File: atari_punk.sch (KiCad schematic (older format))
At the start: 11 parts, among them J1 Conn_01x02_MountingPin, J2 Conn_01x02_MountingPin, U1 NE555P, U2 NE555P

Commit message: Added resistors. Added big Niubit logo. Added holes for mounting.
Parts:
- removed J1, J2: Conn_01x02_MountingPin, Connector_PinHeader_2.54mm:PinHeader_1x02_P2.54mm_Vertical, symbol Connector_Generic_MountingPin:Conn_01x02_MountingPin
- added J1, J2: Conn_01x02_Male, Connector_PinHeader_2.54mm:PinHeader_1x02_P2.54mm_Vertical, symbol Connector:Conn_01x02_Male
- added R5, R6: 1K, Resistor_THT:R_Axial_DIN0207_L6.3mm_D2.5mm_P10.16mm_Horizontal, symbol Device:R
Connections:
- net +9V: now also J1.2 (Pin_2)
- net AUDIO: now also J2.2 (Pin_2)
- net GND: now also J1.1 (Pin_1), J2.1 (Pin_1)
- net at R2.2, U1.7 (DIS): now also R5.1; no longer R1.2
- net at C3.1, U2.6 (THR), U2.7 (DIS): now also R6.1; no longer R4.2
- new net: R1.2, R5.2
- new net: R4.2, R6.2
- no-connect marks 4 -> 2
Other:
- moved on the sheet: R2, R4
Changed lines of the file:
@@
 L Device:R R2
 U 1 1 5FE47346
-P 3000 2500
-F 0 "R2" V 2793 2500 50  0000 C CNN
-F 1 "1K" V 2884 2500 50  0000 C CNN
-F 2 "Resistor_THT:R_Axial_DIN0207_L6.3mm_D2.5mm_P10.16mm_Horizontal" V 2930 2500 50  0001 C CNN
-F 3 "~" H 3000 2500 50  0001 C CNN
-	1    3000 2500
+P 3000 2700
+F 0 "R2" V 2793 2700 50  0000 C CNN
+F 1 "1K" V 2884 2700 50  0000 C CNN
+F 2 "Resistor_THT:R_Axial_DIN0207_L6.3mm_D2.5mm_P10.16mm_Horizontal" V 2930 2700 50  0001 C CNN
+F 3 "~" H 3000 2700 50  0001 C CNN
+	1    3000 2700
 	-1   0    0    1
 $EndComp
@@
 L power:+9V #PWR011
 U 1 1 5FE7EA0E
-P 5200 1450
-F 0 "#PWR011" H 5200 1300 50  0001 C CNN
-F 1 "+9V" H 5215 1623 50  0000 C CNN
-F 2 "" H 5200 1450 50  0001 C CNN
-F 3 "" H 5200 1450 50  0001 C CNN
-	1    5200 1450
+P 5900 1450
+F 0 "#PWR011" H 5900 1300 50  0001 C CNN
+F 1 "+9V" H 5915 1623 50  0000 C CNN
+F 2 "" H 5900 1450 50  0001 C CNN
+F 3 "" H 5900 1450 50  0001 C CNN
+	1    5900 1450
 	1    0    0    -1
 $EndComp
@@
 L Device:R_Variable R4
 U 1 1 5FE4885F
-P 5200 1700
-F 0 "R4" H 5328 1746 50  0000 L CNN
-F 1 "500K" H 5328 1655 50  0000 L CNN
-F 2 "Potentiometer_THT:Potentiometer_Alpha_RD901F-40-00D_Single_Vertical" V 5130 1700 50  0001 C CNN
-F 3 "~" H 5200 1700 50  0001 C CNN
-	1    5200 1700
+P 5900 1700
+F 0 "R4" H 6028 1746 50  0000 L CNN
+F 1 "500K" H 6028 1655 50  0000 L CNN
+F 2 "Potentiometer_THT:Potentiometer_Alpha_RD901F-40-00D_Single_Vertical" V 5830 1700 50  0001 C CNN
+F 3 "~" H 5900 1700 50  0001 C CNN
+	1    5900 1700
 	1    0    0    -1
 $EndComp
@@
 	3000 1450 3000 1550
 Wire Wire Line
-	3000 1850 3000 1950
-Wire Wire Line
-	2550 1950 3000 1950
-Connection ~ 3000 1950
-Wire Wire Line
-	3000 1950 3000 2350
-Wire Wire Line
-	3000 2650 3000 2900
+	3000 2850 3000 2900
 Wire Wire Line
 	3000 2900 2650 2900
@@
 	4800 1950 4900 1950
 Wire Wire Line
-	5200 1950 5200 1850
-Connection ~ 5200 1950
-Wire Wire Line
-	5200 1450 5200 1550
+	5900 1450 5900 1550
 Wire Wire Line
 	5200 2400 5200 2450
@@
 Wire Wire Line
 	4900 1950 5200 1950
-$Comp
-L Connector_Generic_MountingPin:Conn_01x02_MountingPin J1
-U 1 1 5FEDC132
-P 1750 3550
-F 0 "J1" H 1838 3464 50  0000 L CNN
-F 1 "Conn_01x02_MountingPin" H 1450 3650 50  0000 L CNN
-F 2 "Connector_PinHeader_2.54mm:PinHeader_1x02_P2.54mm_Vertical" H 1750 3550 50  0001 C CNN
-F 3 "~" H 1750 3550 50  0001 C CNN
-	1    1750 3550
-	-1   0    0    1
-$EndComp
-$Comp
-L Connector_Generic_MountingPin:Conn_01x02_MountingPin J2
-U 1 1 5FEDD85A
-P 4350 3550
-F 0 "J2" H 4438 3464 50  0000 L CNN
-F 1 "Conn_01x02_MountingPin" H 4050 3650 50  0000 L CNN
-F 2 "Connector_PinHeader_2.54mm:PinHeader_1x02_P2.54mm_Vertical" H 4350 3550 50  0001 C CNN
-F 3 "~" H 4350 3550 50  0001 C CNN
-	1    4350 3550
-	-1   0    0    1
-$EndComp
 $Comp
 L power:+9V #PWR01
@@
 	1    0    0    -1
 $EndComp
-Text GLabel 4800 3450 2    50   Input ~ 0
+Text GLabel 4800 3450 0    50   Input ~ 0
 AUDIO
 Text GLabel 5750 1000 2    50   Output ~ 0
@@
 	5350 1000 5750 1000
 Wire Wire Line
-	1950 3550 2150 3550
+	4800 3550 4800 3650
+$Comp
+L Device:R R5
+U 1 1 608860B0
+P 3000 2100
+F 0 "R5" V 2793 2100 50  0000 C CNN
+F 1 "1K" V 2884 2100 50  0000 C CNN
+F 2 "Resistor_THT:R_Axial_DIN0207_L6.3mm_D2.5mm_P10.16mm_Horizontal" V 2930 2100 50  0001 C CNN
+F 3 "~" H 3000 2100 50  0001 C CNN
+	1    3000 2100
+	-1   0    0    1
+$EndComp
+Wire Wire Line
+	3000 1950 3000 1850
+Wire Wire Line
+	3000 2250 3000 2400
+Wire Wire Line
+	2550 1950 2800 1950
+Wire Wire Line
+	2800 1950 2800 2400
+Wire Wire Line
+	2800 2400 3000 2400
+Connection ~ 3000 2400
+Wire Wire Line
+	3000 2400 3000 2550
+$Comp
+L Device:R R6
+U 1 1 6089116C
+P 5600 1950
+F 0 "R6" V 5393 1950 50  0000 C CNN
+F 1 "1K" V 5484 1950 50  0000 C CNN
+F 2 "Resistor_THT:R_Axial_DIN0207_L6.3mm_D2.5mm_P10.16mm_Horizontal" V 5530 1950 50  0001 C CNN
+F 3 "~" H 5600 1950 50  0001 C CNN
+	1    5600 1950
+	0    -1   -1   0
+$EndComp
+Wire Wire Line
+	5900 1850 5900 1950
+Wire Wire Line
+	5900 1950 5750 1950
+Wire Wire Line
+	5450 1950 5200 1950
+Connection ~ 5200 1950
+$Comp
+L Connector:Conn_01x02_Male J1
+U 1 1 60897D2C
+P 2550 3550
+F 0 "J1" H 2522 3432 50  0000 R CNN
+F 1 "Conn_01x02_Male" H 2522 3523 50  0000 R CNN
+F 2 "Connector_PinHeader_2.54mm:PinHeader_1x02_P2.54mm_Vertical" H 2550 3550 50  0001 C CNN
+F 3 "~" H 2550 3550 50  0001 C CNN
+	1    2550 3550
+	-1   0    0    1
+$EndComp
+Wire Wire Line
+	2350 3450 2150 3450
+Wire Wire Line
+	2150 3450 2150 3350
+Wire Wire Line
+	2350 3550 2150 3550
 Wire Wire Line
 	2150 3550 2150 3650
-Wire Wire Line
-	1950 3450 2150 3450
-Wire Wire Line
-	2150 3450 2150 3350
-NoConn ~ 1750 3250
-Wire Wire Line
-	4550 3450 4800 3450
-Wire Wire Line
-	4550 3550 4800 3550
-Wire Wire Line
-	4800 3550 4800 3650
-NoConn ~ 4350 3250
+$Comp
+L Connector:Conn_01x02_Male J2
+U 1 1 6089F405
+P 5250 3550
+F 0 "J2" H 5222 3432 50  0000 R CNN
+F 1 "Conn_01x02_Male" H 5222 3523 50  0000 R CNN
+F 2 "Connector_PinHeader_2.54mm:PinHeader_1x02_P2.54mm_Vertical" H 5250 3550 50  0001 C CNN
+F 3 "~" H 5250 3550 50  0001 C CNN
+	1    5250 3550
+	-1   0    0    1
+$EndComp
+Wire Wire Line
+	5050 3450 4800 3450
+Wire Wire Line
+	5050 3550 4800 3550
 $EndSCHEMATC

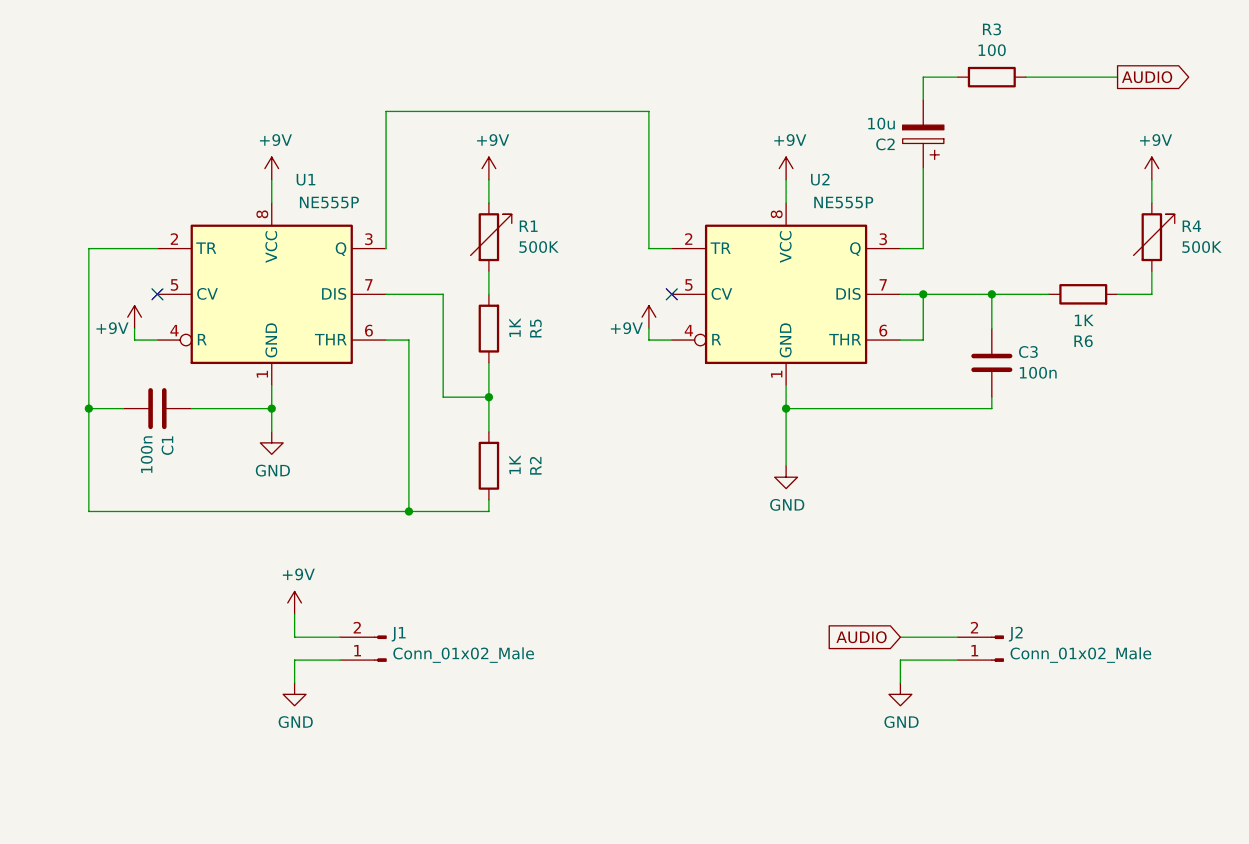
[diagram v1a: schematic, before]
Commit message: Se incorpora interruptor de encendido.
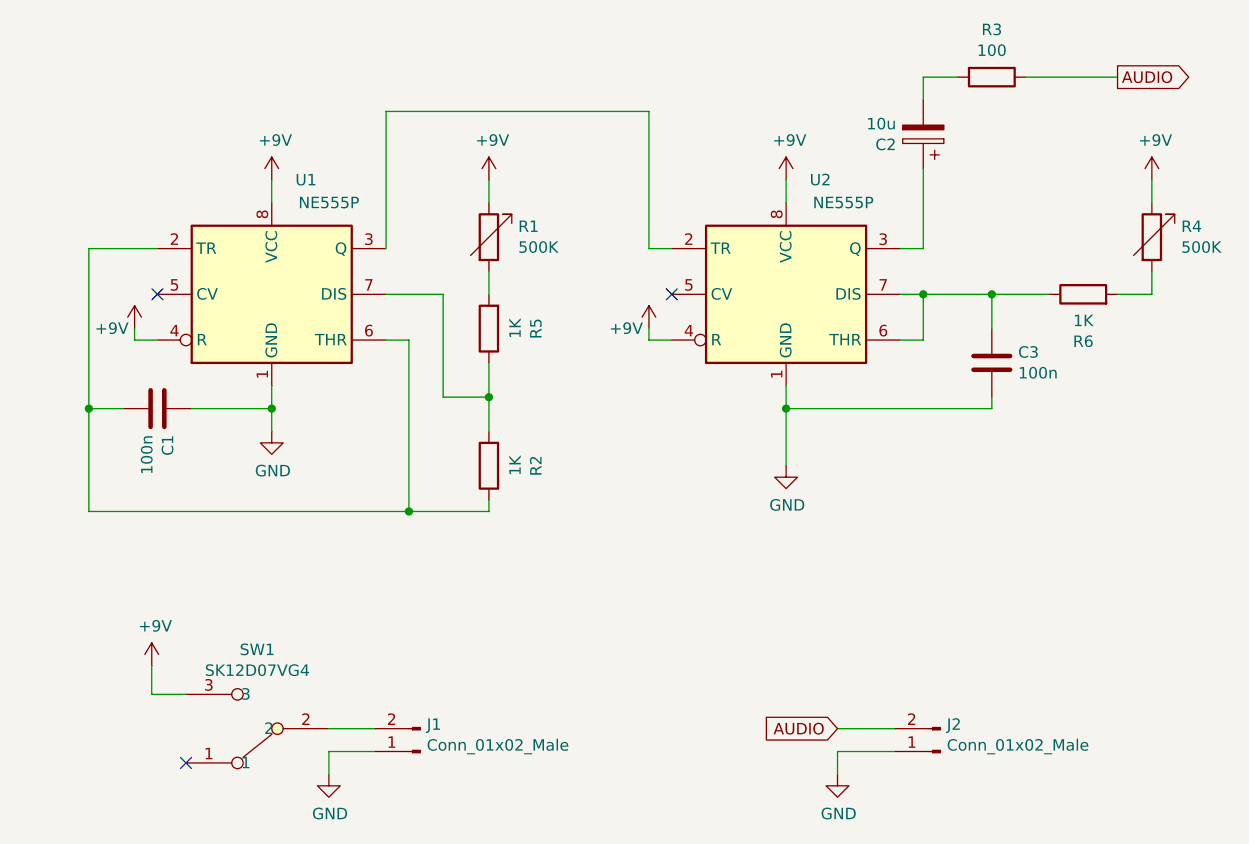
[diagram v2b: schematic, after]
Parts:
- added SW1: SK12D07VG4, Button_Switch_THT:SW_CuK_OS102011MA1QN1_SPDT_Angled, symbol eduardofilo_symbols:SK12D07VG4
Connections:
- net +9V: now also SW1.3; no longer J1.2 (Pin_2)
- new net: J1.2 (Pin_2), SW1.2
- no-connect marks 2 -> 3
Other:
- moved on the sheet: J1, J2
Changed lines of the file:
@@
 L power:+9V #PWR01
 U 1 1 5FEDDCAC
-P 2150 3350
-F 0 "#PWR01" H 2150 3200 50  0001 C CNN
-F 1 "+9V" H 2165 3523 50  0000 C CNN
-F 2 "" H 2150 3350 50  0001 C CNN
-F 3 "" H 2150 3350 50  0001 C CNN
-	1    2150 3350
+P 1525 3575
+F 0 "#PWR01" H 1525 3425 50  0001 C CNN
+F 1 "+9V" H 1540 3748 50  0000 C CNN
+F 2 "" H 1525 3575 50  0001 C CNN
+F 3 "" H 1525 3575 50  0001 C CNN
+	1    1525 3575
 	1    0    0    -1
 $EndComp
@@
 L power:GND #PWR02
 U 1 1 5FEDE15B
-P 2150 3650
-F 0 "#PWR02" H 2150 3400 50  0001 C CNN
-F 1 "GND" H 2155 3477 50  0000 C CNN
-F 2 "" H 2150 3650 50  0001 C CNN
-F 3 "" H 2150 3650 50  0001 C CNN
-	1    2150 3650
+P 2300 4050
+F 0 "#PWR02" H 2300 3800 50  0001 C CNN
+F 1 "GND" H 2305 3877 50  0000 C CNN
+F 2 "" H 2300 4050 50  0001 C CNN
+F 3 "" H 2300 4050 50  0001 C CNN
+	1    2300 4050
 	1    0    0    -1
 $EndComp
@@
 L power:GND #PWR08
 U 1 1 5FEDF6E2
-P 4800 3650
-F 0 "#PWR08" H 4800 3400 50  0001 C CNN
-F 1 "GND" H 4805 3477 50  0000 C CNN
-F 2 "" H 4800 3650 50  0001 C CNN
-F 3 "" H 4800 3650 50  0001 C CNN
-	1    4800 3650
+P 4525 4050
+F 0 "#PWR08" H 4525 3800 50  0001 C CNN
+F 1 "GND" H 4530 3877 50  0000 C CNN
+F 2 "" H 4525 4050 50  0001 C CNN
+F 3 "" H 4525 4050 50  0001 C CNN
+	1    4525 4050
 	1    0    0    -1
 $EndComp
-Text GLabel 4800 3450 0    50   Input ~ 0
+Text GLabel 4525 3850 0    50   Input ~ 0
 AUDIO
 Text GLabel 5750 1000 2    50   Output ~ 0
@@
 	5350 1000 5750 1000
 Wire Wire Line
-	4800 3550 4800 3650
+	4525 3950 4525 4050
 $Comp
 L Device:R R5
@@
 L Connector:Conn_01x02_Male J1
 U 1 1 60897D2C
-P 2550 3550
-F 0 "J1" H 2522 3432 50  0000 R CNN
-F 1 "Conn_01x02_Male" H 2522 3523 50  0000 R CNN
-F 2 "Connector_PinHeader_2.54mm:PinHeader_1x02_P2.54mm_Vertical" H 2550 3550 50  0001 C CNN
-F 3 "~" H 2550 3550 50  0001 C CNN
-	1    2550 3550
+P 2700 3950
+F 0 "J1" H 2672 3832 50  0000 R CNN
+F 1 "Conn_01x02_Male" H 2672 3923 50  0000 R CNN
+F 2 "Connector_PinHeader_2.54mm:PinHeader_1x02_P2.54mm_Vertical" H 2700 3950 50  0001 C CNN
+F 3 "~" H 2700 3950 50  0001 C CNN
+	1    2700 3950
 	-1   0    0    1
 $EndComp
 Wire Wire Line
-	2350 3450 2150 3450
+	2500 3950 2300 3950
 Wire Wire Line
-	2150 3450 2150 3350
-Wire Wire Line
-	2350 3550 2150 3550
-Wire Wire Line
-	2150 3550 2150 3650
+	2300 3950 2300 4050
 $Comp
 L Connector:Conn_01x02_Male J2
 U 1 1 6089F405
-P 5250 3550
-F 0 "J2" H 5222 3432 50  0000 R CNN
-F 1 "Conn_01x02_Male" H 5222 3523 50  0000 R CNN
-F 2 "Connector_PinHeader_2.54mm:PinHeader_1x02_P2.54mm_Vertical" H 5250 3550 50  0001 C CNN
-F 3 "~" H 5250 3550 50  0001 C CNN
-	1    5250 3550
+P 4975 3950
+F 0 "J2" H 4947 3832 50  0000 R CNN
+F 1 "Conn_01x02_Male" H 4947 3923 50  0000 R CNN
+F 2 "Connector_PinHeader_2.54mm:PinHeader_1x02_P2.54mm_Vertical" H 4975 3950 50  0001 C CNN
+F 3 "~" H 4975 3950 50  0001 C CNN
+	1    4975 3950
 	-1   0    0    1
 $EndComp
 Wire Wire Line
-	5050 3450 4800 3450
+	4775 3850 4525 3850
 Wire Wire Line
-	5050 3550 4800 3550
+	4775 3950 4525 3950
+$Comp
+L eduardofilo_symbols:SK12D07VG4 SW1
+U 1 1 608B1CDF
+P 1900 3850
+F 0 "SW1" H 1813 3505 50  0000 C CNN
+F 1 "SK12D07VG4" H 1813 3596 50  0000 C CNN
+F 2 "Button_Switch_THT:SW_CuK_OS102011MA1QN1_SPDT_Angled" H 1925 3950 50  0001 C CNN
+F 3 "" H 1925 3950 50  0001 C CNN
+	1    1900 3850
+	-1   0    0    1
+$EndComp
+Wire Wire Line
+	2500 3850 2300 3850
+Wire Wire Line
+	1675 3700 1525 3700
+Wire Wire Line
+	1525 3700 1525 3575
+NoConn ~ 1675 4000
 $EndSCHEMATC

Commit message: Se agrandan los pad de chasis de los potenciómetros.
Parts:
- R1, R4: footprint Potentiometer_THT:Potentiometer_Alpha_RD901F-40-00D_Single_Vertical -> eduardofilo_footprints:Potentiometer_Alpha_RD901F-40-00D_Single_Vertical_mod
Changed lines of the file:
@@
 F 0 "R1" H 3128 1746 50  0000 L CNN
 F 1 "500K" H 3128 1655 50  0000 L CNN
-F 2 "Potentiometer_THT:Potentiometer_Alpha_RD901F-40-00D_Single_Vertical" V 2930 1700 50  0001 C CNN
+F 2 "eduardofilo_footprints:Potentiometer_Alpha_RD901F-40-00D_Single_Vertical_mod" V 2930 1700 50  0001 C CNN
 F 3 "~" H 3000 1700 50  0001 C CNN
 	1    3000 1700
@@
 F 0 "R4" H 6028 1746 50  0000 L CNN
 F 1 "500K" H 6028 1655 50  0000 L CNN
-F 2 "Potentiometer_THT:Potentiometer_Alpha_RD901F-40-00D_Single_Vertical" V 5830 1700 50  0001 C CNN
+F 2 "eduardofilo_footprints:Potentiometer_Alpha_RD901F-40-00D_Single_Vertical_mod" V 5830 1700 50  0001 C CNN
 F 3 "~" H 5900 1700 50  0001 C CNN
 	1    5900 1700
